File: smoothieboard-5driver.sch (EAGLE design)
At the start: 274 parts, among them IC1 LPC1769, IC10 LM1117-3.3V, IC11 78L12F, IC12 A4982, IC2 A4982, IC3 A4982, IC4 MCP44X1, IC5 A4982, IC6 A4982, IC9 MCP44X1, J10 POWER_JACKSMD, Q1 BSL207SP, Q10 SUD50P04-08-GE3, Q2 12MHz, Q3 25MHz, Q4 ZXMN4A06, Q5 AOT240L, Q6 AOT240L, Q7 AOT240L, Q8 ZXMN4A06, Q9 ZXMN4A06, U1 USD-SOCKETNEW, X14 USBPTH

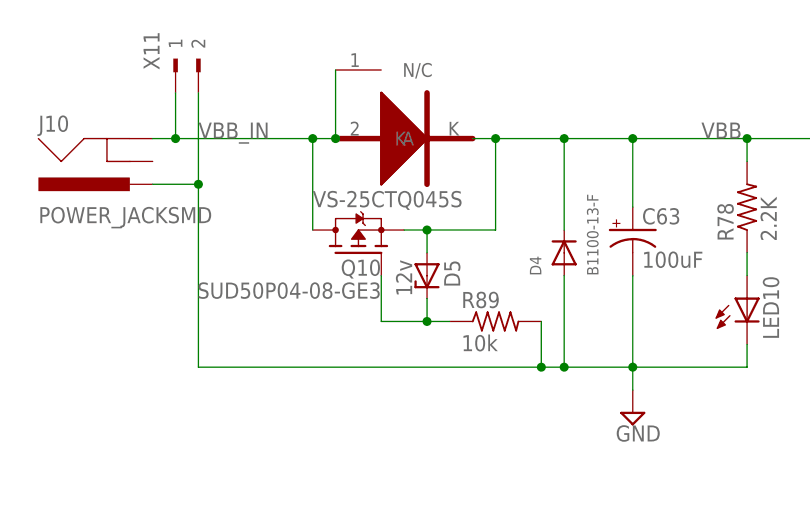
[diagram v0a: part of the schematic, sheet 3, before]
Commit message: add some heatsinking for reverse polarity mosfet on back of board using thermal vias
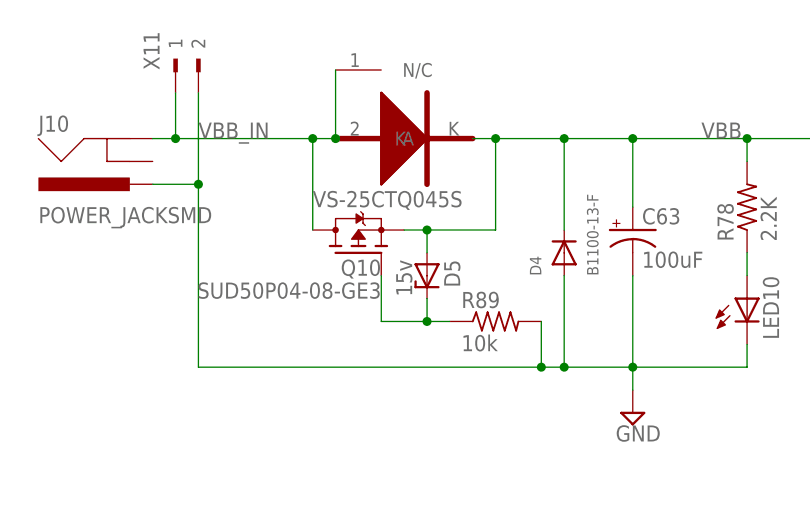
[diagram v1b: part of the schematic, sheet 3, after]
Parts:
- D5: value 12v -> 15v
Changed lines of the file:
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@@
 <part name="Q10" library="transistor-fet" deviceset="SPD30P06P" device="TO252" value="SUD50P04-08-GE3"/>
 <part name="R89" library="resistor" deviceset="R-US_" device="R0603" value="10k"/>
-<part name="D5" library="diode" deviceset="ZENER-DIODE" device="SMB" value="12v"/>
+<part name="D5" library="diode" deviceset="ZENER-DIODE" device="SMB" value="15v"/>
 </parts>
 <sheets>

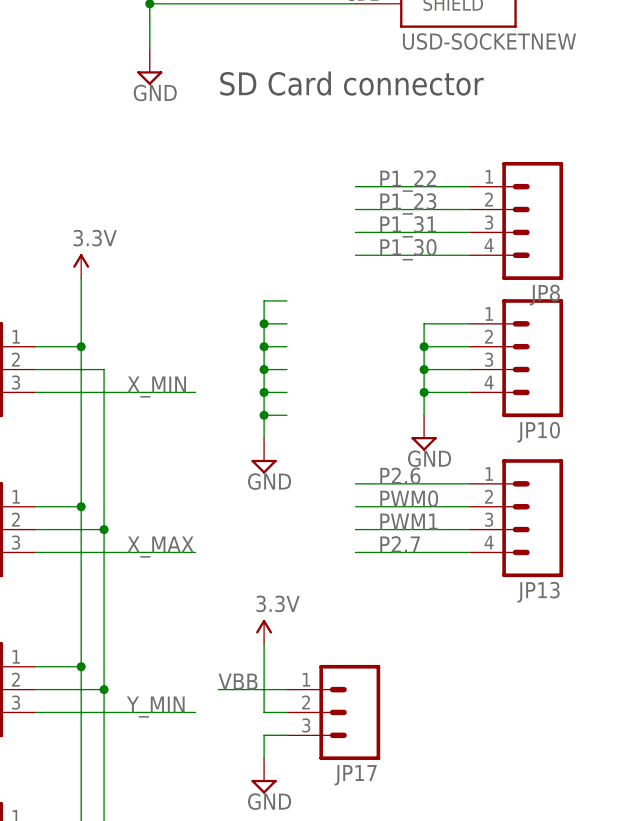
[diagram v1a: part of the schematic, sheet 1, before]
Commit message: Silkscreen text added- M5, VBB, +5v etc part names adjusted Q8 and Q9 aligned 3.5mm footprints added to new mosfets and power input JP32/33 added with ground pins plus necessary rerouting C40 changed to 45 degrees
probably other misc tweaks and fixes
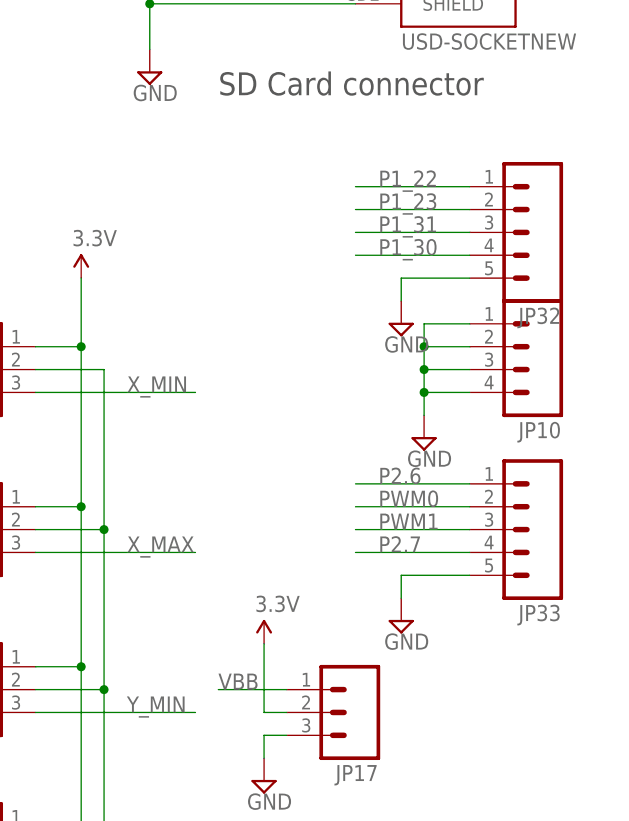
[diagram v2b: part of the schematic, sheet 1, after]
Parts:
- removed JP13, JP8: (no value), SparkFun:M041X04_NO_SILK
- added J11, J12: (no value), con-amp:MTA02-100
- added JP32, JP33: (no value), SparkFun:M05PTH
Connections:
- net GND: now also J12.2, JP32.5, JP33.5
- net MOSFET_DRIVE1: now also J11.1, J12.1
- net N$109: now also J11.2
- net P1_22: now also JP32.1; no longer JP8.1
- net P1_23: now also JP32.2; no longer JP8.2
- net P1_30: now also JP32.4; no longer JP8.4
- net P1_31: now also JP32.3; no longer JP8.3
- net P2.6: now also JP33.1; no longer JP13.1
- net P2.7: now also JP33.4; no longer JP13.4
- net PWM0: now also JP33.2; no longer JP13.2
- net PWM1: now also JP33.3; no longer JP13.3

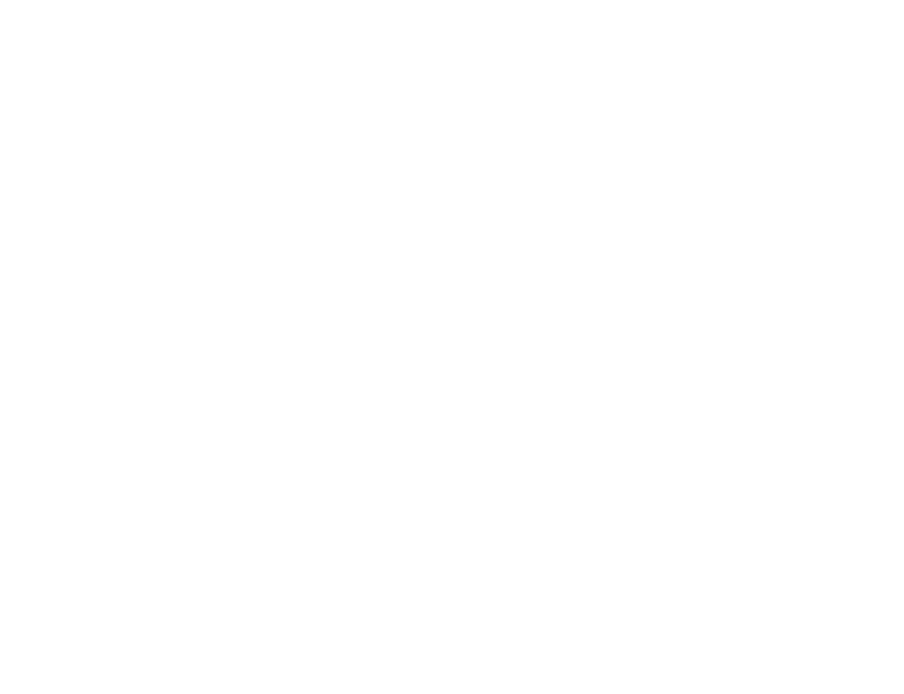
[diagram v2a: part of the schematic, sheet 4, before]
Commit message: added footprint for optional R-78E-5.0 dc-dc converter for converting from VBB to 5V
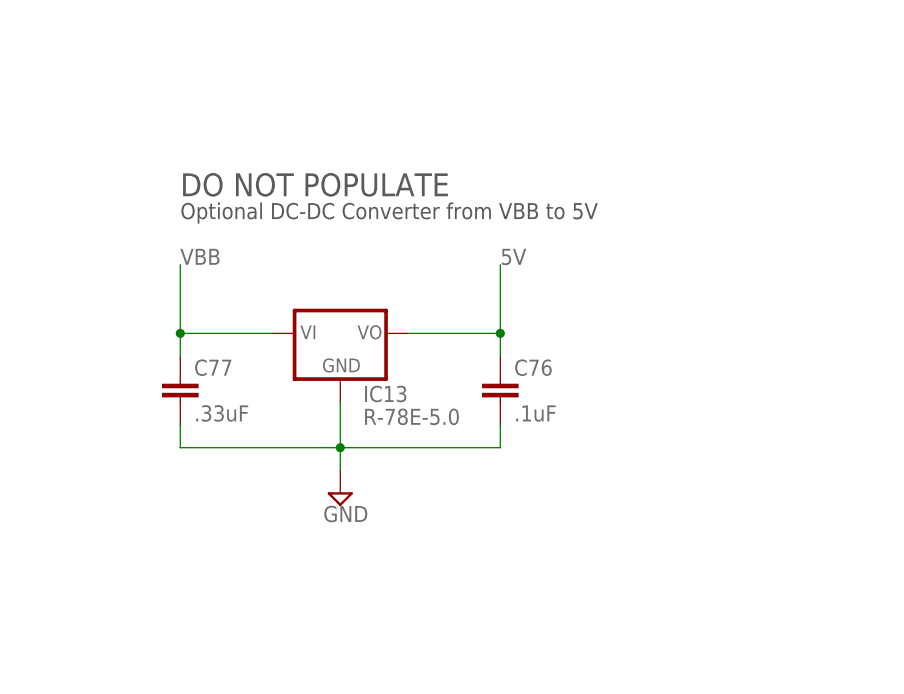
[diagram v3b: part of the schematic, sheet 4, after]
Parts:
- added C76: .1uF, rcl:C-EUC0603
- added C77: .33uF, rcl:C-EUC0603
- added IC13: R-78E-5.0, logxen:R-78
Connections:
- net 5V: now also C76.1, IC13.VO
- net GND: now also C76.2, C77.2, IC13.GND
- net VBB: now also C77.1, IC13.VI
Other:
- note added: "DO NOT POPULATE"
- note added: "Optional DC-DC Converter from VBB to 5V"

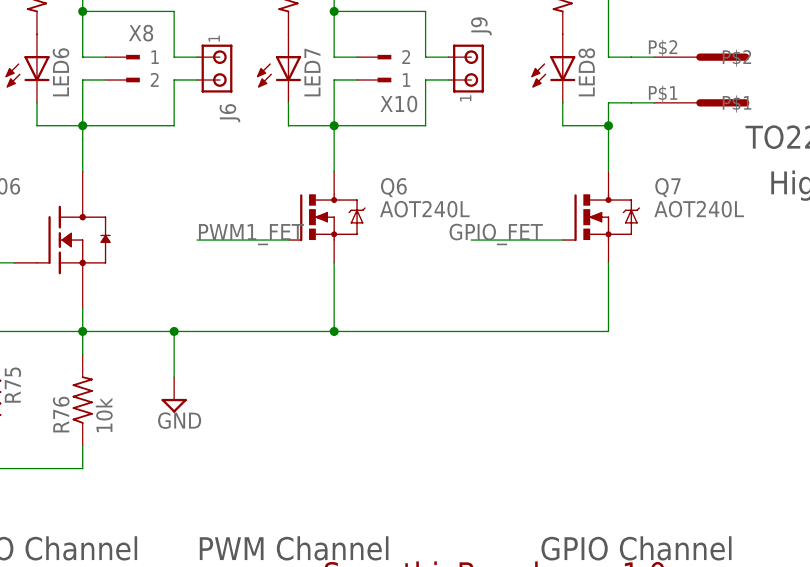
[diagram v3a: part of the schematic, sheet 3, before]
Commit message: add pull-downs on large mosfet gates, tons of silkscreen tidying including labelling of signals in connectors and power routing indicators
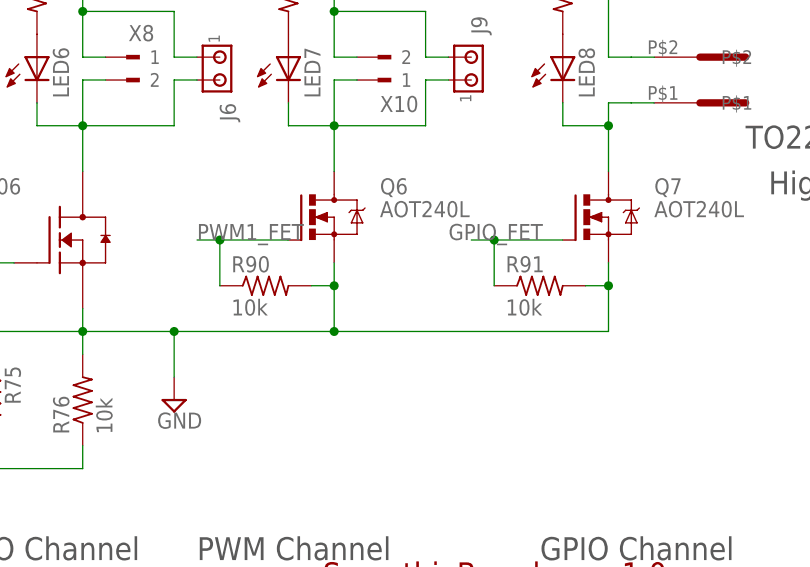
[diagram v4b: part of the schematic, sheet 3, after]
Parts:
- added R90, R91: 10k, resistor:R-US_R0603
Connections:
- net GND: now also R90.2, R91.2
- net GPIO_FET: now also R91.1
- net PWM1_FET: now also R90.1
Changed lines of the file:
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@@
 <?xml version="1.0" encoding="utf-8"?>
 <!DOCTYPE eagle SYSTEM "eagle.dtd">
-<eagle version="6.3">
+<eagle version="6.2">
 <drawing>
 <settings>
@@
 <part name="C76" library="rcl" deviceset="C-EU" device="C0603" value=".1uF"/>
 <part name="C77" library="rcl" deviceset="C-EU" device="C0603" value=".33uF"/>
+<part name="R90" library="resistor" deviceset="R-US_" device="R0603" value="10k"/>
+<part name="R91" library="resistor" deviceset="R-US_" device="R0603" value="10k"/>
 </parts>
 <sheets>
@@
 <instance part="R89" gate="G$1" x="160.02" y="22.86"/>
 <instance part="D5" gate="G$1" x="152.4" y="27.94" rot="R270"/>
+<instance part="R90" gate="G$1" x="292.1" y="66.04"/>
+<instance part="R91" gate="G$1" x="322.58" y="66.04"/>
 </instances>
 <busses>
@@
 <wire x1="281.94" y1="60.96" x2="299.72" y2="60.96" width="0.4064" layer="91"/>
 <wire x1="299.72" y1="60.96" x2="330.2" y2="60.96" width="0.4064" layer="91"/>
-<wire x1="330.2" y1="60.96" x2="330.2" y2="68.58" width="0.4064" layer="91"/>
-<wire x1="299.72" y1="68.58" x2="299.72" y2="60.96" width="0.4064" layer="91"/>
+<wire x1="330.2" y1="60.96" x2="330.2" y2="66.04" width="0.4064" layer="91"/>
+<wire x1="330.2" y1="66.04" x2="330.2" y2="68.58" width="0.4064" layer="91"/>
+<wire x1="299.72" y1="68.58" x2="299.72" y2="66.04" width="0.4064" layer="91"/>
+<wire x1="299.72" y1="66.04" x2="299.72" y2="60.96" width="0.4064" layer="91"/>
 <wire x1="271.78" y1="63.5" x2="271.78" y2="60.96" width="0.4064" layer="91"/>
 <wire x1="281.94" y1="55.88" x2="281.94" y2="60.96" width="0.1524" layer="91"/>
@@
 <pinref part="R74" gate="G$1" pin="2"/>
 <pinref part="R76" gate="G$1" pin="2"/>
+<pinref part="R90" gate="G$1" pin="2"/>
+<wire x1="297.18" y1="66.04" x2="299.72" y2="66.04" width="0.1524" layer="91"/>
+<junction x="299.72" y="66.04"/>
+<pinref part="R91" gate="G$1" pin="2"/>
+<wire x1="327.66" y1="66.04" x2="330.2" y2="66.04" width="0.1524" layer="91"/>
+<junction x="330.2" y="66.04"/>
 </segment>
 <segment>
@@
 <segment>
 <pinref part="Q6" gate="G$1" pin="G"/>
-<wire x1="294.64" y1="71.12" x2="284.48" y2="71.12" width="0.1524" layer="91"/>
+<wire x1="294.64" y1="71.12" x2="287.02" y2="71.12" width="0.1524" layer="91"/>
 <label x="284.48" y="71.12" size="1.778" layer="95"/>
+<pinref part="R90" gate="G$1" pin="1"/>
+<wire x1="287.02" y1="71.12" x2="284.48" y2="71.12" width="0.1524" layer="91"/>
+<wire x1="287.02" y1="66.04" x2="287.02" y2="71.12" width="0.1524" layer="91"/>
+<junction x="287.02" y="71.12"/>
 </segment>
 </net>
@@
 <segment>
 <pinref part="Q7" gate="G$1" pin="G"/>
-<wire x1="325.12" y1="71.12" x2="314.96" y2="71.12" width="0.1524" layer="91"/>
+<wire x1="325.12" y1="71.12" x2="317.5" y2="71.12" width="0.1524" layer="91"/>
 <label x="312.42" y="71.12" size="1.778" layer="95"/>
+<pinref part="R91" gate="G$1" pin="1"/>
+<wire x1="317.5" y1="71.12" x2="314.96" y2="71.12" width="0.1524" layer="91"/>
+<wire x1="317.5" y1="66.04" x2="317.5" y2="71.12" width="0.1524" layer="91"/>
+<junction x="317.5" y="71.12"/>
 </segment>
 </net>

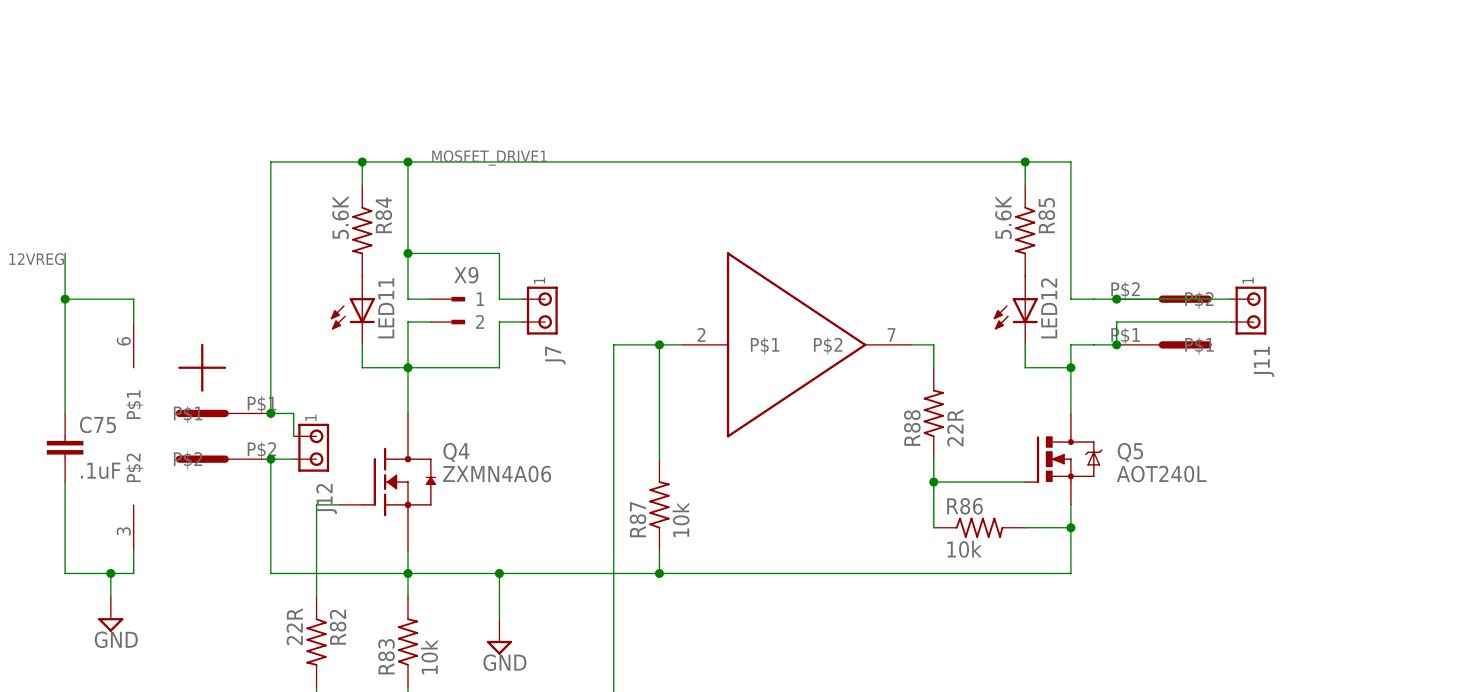
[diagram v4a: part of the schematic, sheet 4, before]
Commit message: ensure all connectors include a 3.5mm footprint, remove 0.1" footprint from high current connector, minor routing updates
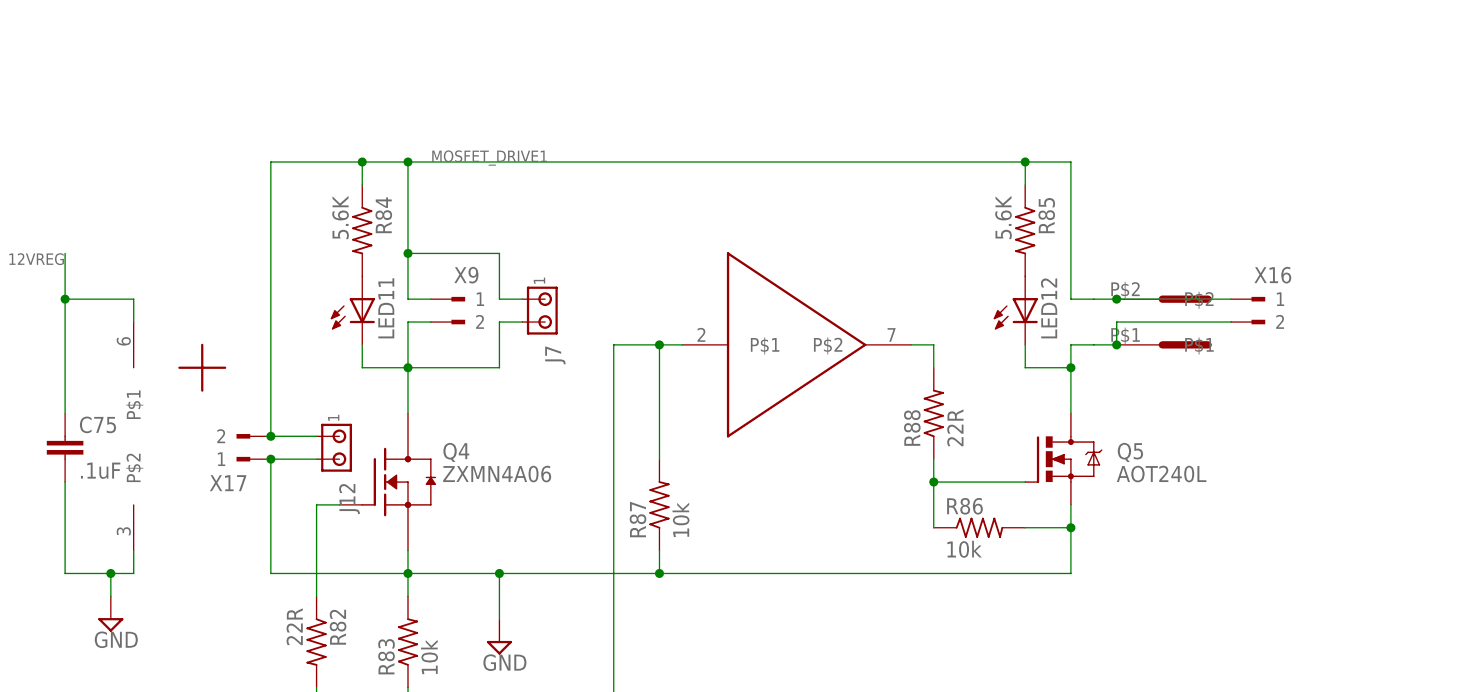
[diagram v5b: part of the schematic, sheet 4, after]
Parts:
- removed J11: (no value), con-amp:MTA02-100
- removed U$9: 5MMCONN, eric_sorensen:5MMCONN
- added X13, X15, X16, X17: (no value), con-weidmueller-sl35:180G-2
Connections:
- net GND: now also X13.2, X17.1; no longer U$9.P$2
- net MOSFET_DRIVE: now also X13.1, X15.2
- net MOSFET_DRIVE1: now also X16.1, X17.2; no longer J11.1, U$9.P$1
- net N$109: now also X16.2; no longer J11.2
- net N$94: now also X15.1
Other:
- moved on the sheet: J12
